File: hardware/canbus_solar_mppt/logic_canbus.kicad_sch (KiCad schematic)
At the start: 29 parts

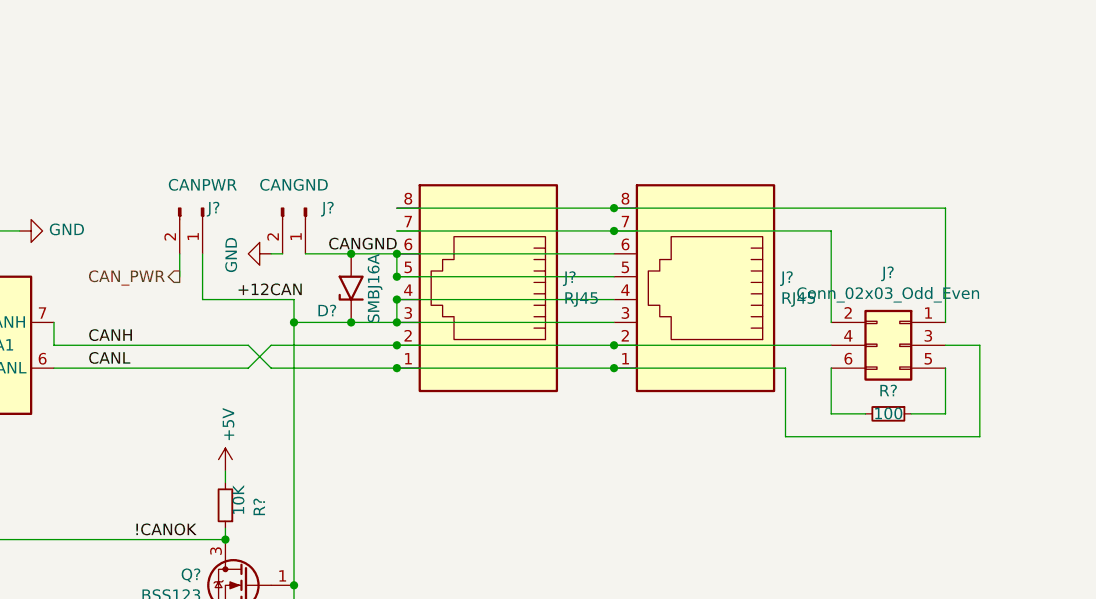
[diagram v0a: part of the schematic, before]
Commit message: Add feedthrough capacitors as EMI filters on power inputs
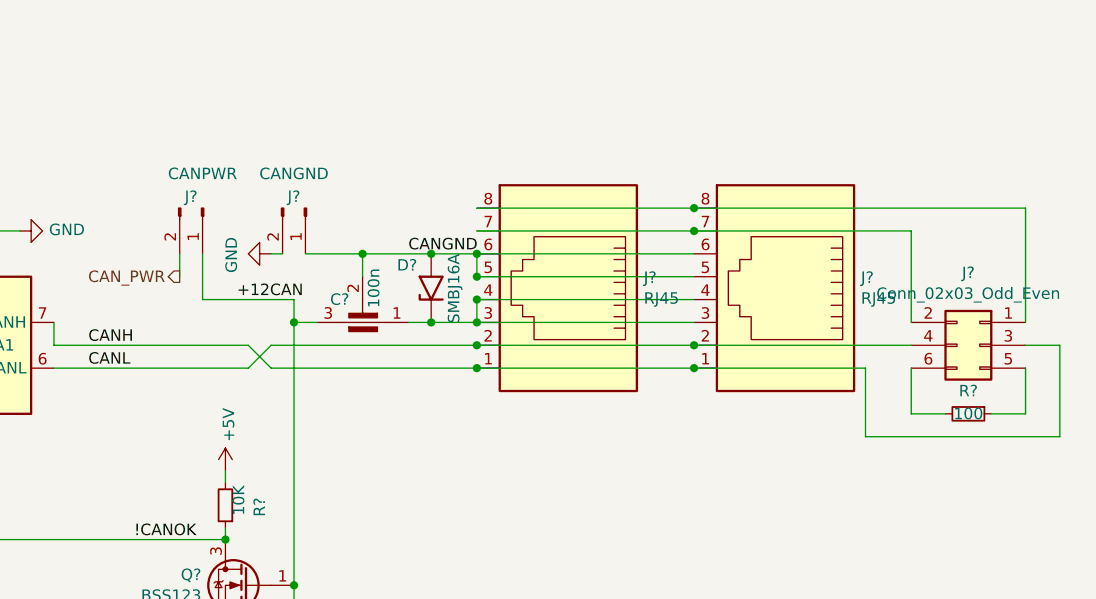
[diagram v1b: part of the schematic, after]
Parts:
- added C?: 100n, local:C_filter_0805, symbol Device:C_Feedthrough
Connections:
- net +12CAN: now also C?.3; no longer D?.1 (A1), J?.3, J?.3, J?.4, J?.4
- net CANGND: now also C?.2
- new net: C?.1, D?.1 (A1), J?.3, J?.3, J?.4, J?.4
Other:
- moved on the sheet: D?, J?, R?

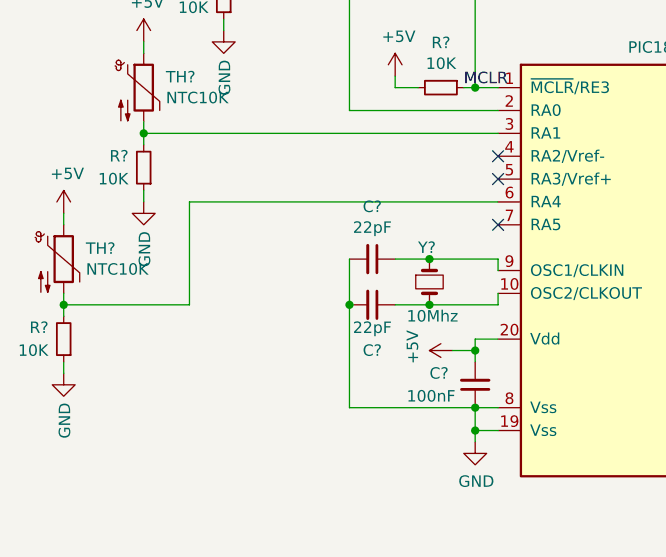
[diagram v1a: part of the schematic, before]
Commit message: Add a voltage reference for the pic18 comparator, and a matching voltage divider at DC/DC output.
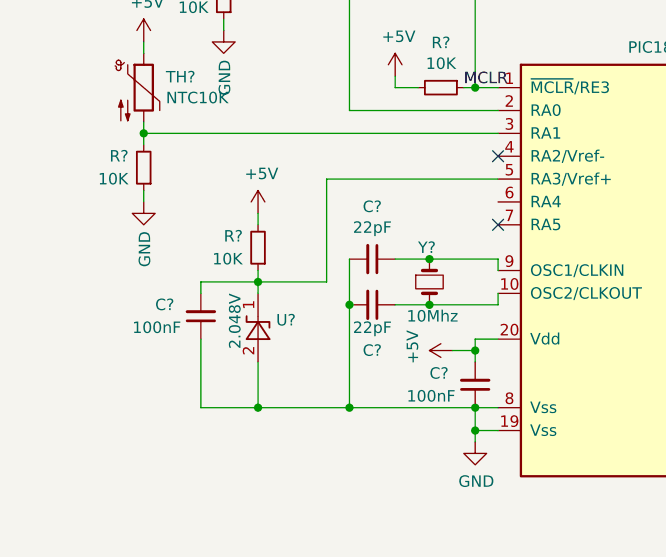
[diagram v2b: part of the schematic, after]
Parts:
- removed R?: 10K, Resistor_SMD:R_1206_3216Metric_Pad1.30x1.75mm_HandSolder, symbol Device:R_Small
- removed TH?: NTC10K, TerminalBlock_TE-Connectivity:TerminalBlock_TE_282834-2_1x02_P2.54mm_Horizontal, symbol Device:Thermistor_NTC
- added C?: 100nF, Capacitor_SMD:C_0805_2012Metric_Pad1.18x1.45mm_HandSolder, symbol Device:C_Small
- added R?: 10K, Resistor_SMD:R_1206_3216Metric_Pad1.30x1.75mm_HandSolder, symbol Device:R_Small
- added U?: 2.048V, Package_TO_SOT_SMD:SOT-23, symbol Reference_Voltage:LM4040DBZ-2.0
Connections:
- net +5V: now also R?.2
- net GND: now also C?.1, U?.2 (A)
- net at U?.5 (RA3/Vref+): now also C?.2, R?.1, U?.1 (K)
- no-connect marks 3 -> 2

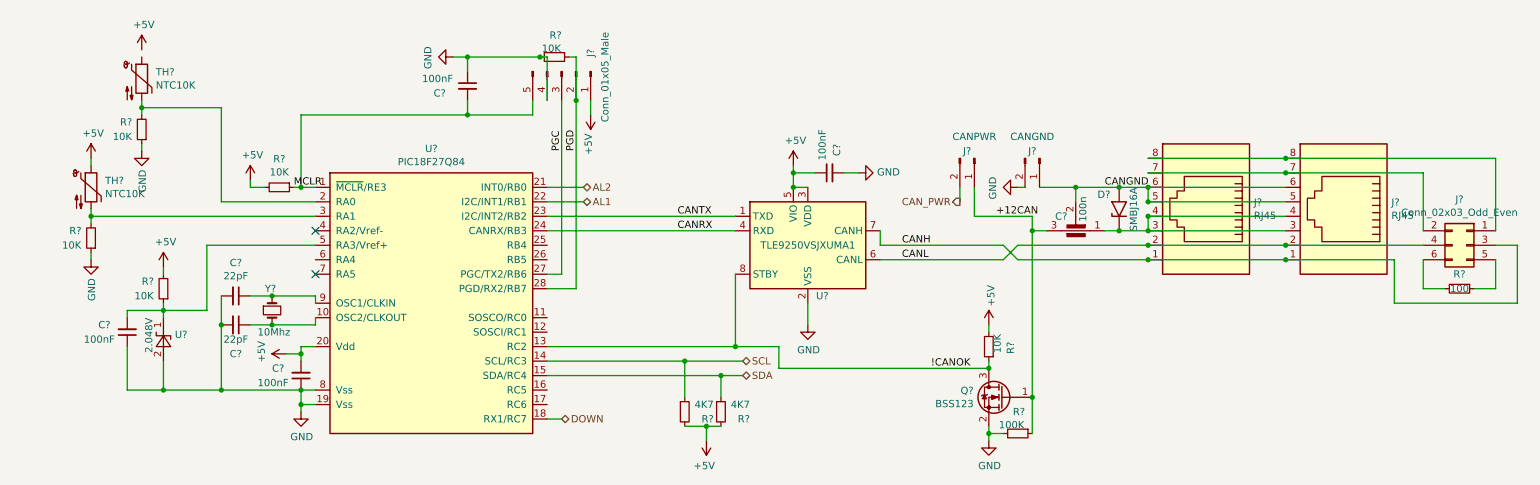
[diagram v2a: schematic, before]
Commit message: Add more signals between pic18 and DC/DC
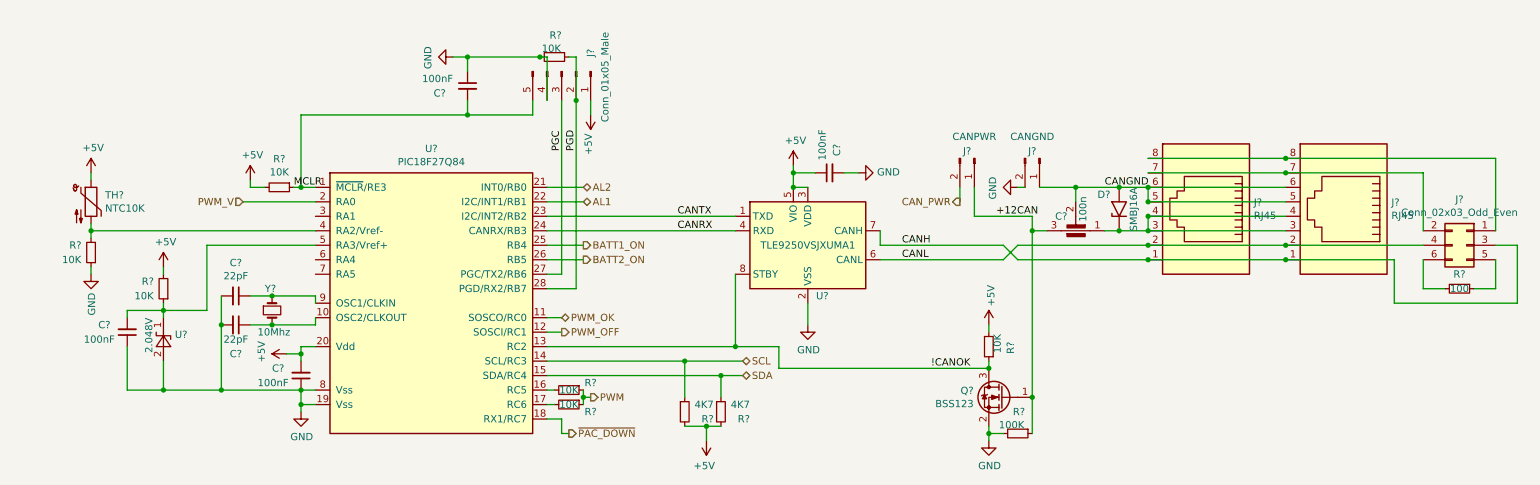
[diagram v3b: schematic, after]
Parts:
- removed R?: 10K, Resistor_SMD:R_1206_3216Metric_Pad1.30x1.75mm_HandSolder, symbol Device:R_Small
- removed TH?: NTC10K, TerminalBlock_TE-Connectivity:TerminalBlock_TE_282834-2_1x02_P2.54mm_Horizontal, symbol Device:Thermistor_NTC
- added R? (x2): 10K, Resistor_THT:R_Axial_DIN0207_L6.3mm_D2.5mm_P7.62mm_Horizontal, symbol Device:R_Small
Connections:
- net PWM_OK: now reaches U?.11 (SOSCO/RC0)
- net PWM_OFF: now reaches U?.12 (SOSCI/RC1)
- net at U?.16 (RC5): now also R?.2
- net at U?.17 (RC6): now also R?.2
- net PWM_V: now reaches U?.2 (RA0)
- net BATT1_ON: now reaches U?.25 (RB4)
- net BATT2_ON: now reaches U?.26 (RB5)
- net at R?.2, TH?.2: now also U?.4 (RA2/Vref-); no longer U?.3 (RA1)
- net DOWN renamed ~{PAC_DOWN}
- new net PWM: R?.1, R?.1
- no-connect marks 2 -> 0
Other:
- moved on the sheet: R?, TH?

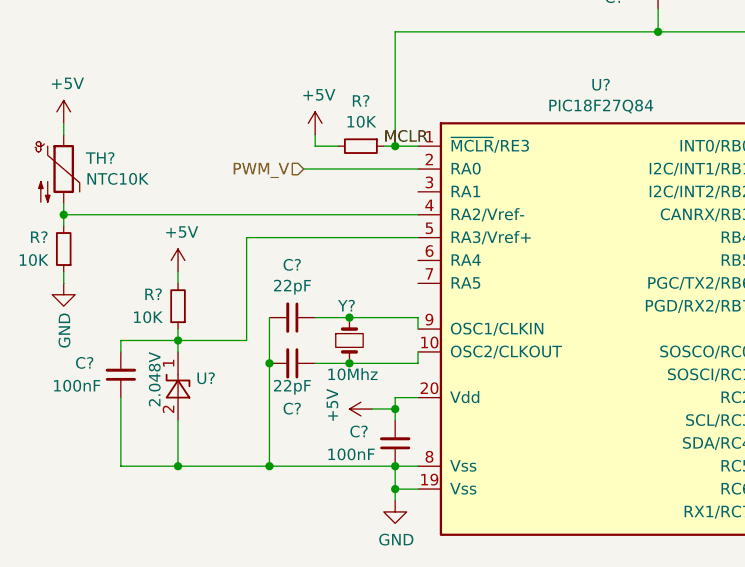
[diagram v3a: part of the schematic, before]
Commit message: Add MCOB12864JX oled display. I2C-connected, not enough pic18 pins for SPI ...
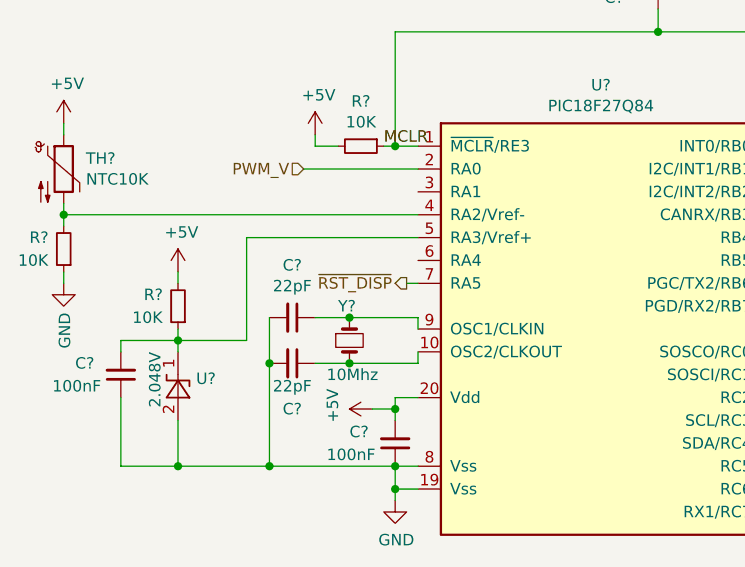
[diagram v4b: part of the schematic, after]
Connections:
- net ~{RST_DISP}: now reaches U?.7 (RA5)
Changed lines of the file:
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@@
+    (stroke (width 0) (type default) (color 0 0 0 0))
+  )
+  (wire (pts (xy 69.85 87.63) (xy 71.12 87.63))
     (stroke (width 0) (type default) (color 0 0 0 0))
   )
@@
     (effects (font (size 1.27 1.27)) (justify left))
   )
+  (hierarchical_label "~{RST_DISP}" (shape output) (at 69.85 87.63 180)
+    (effects (font (size 1.27 1.27)) (justify right))
+  )
   (hierarchical_label "SDA" (shape bidirectional) (at 146.05 105.41 0)

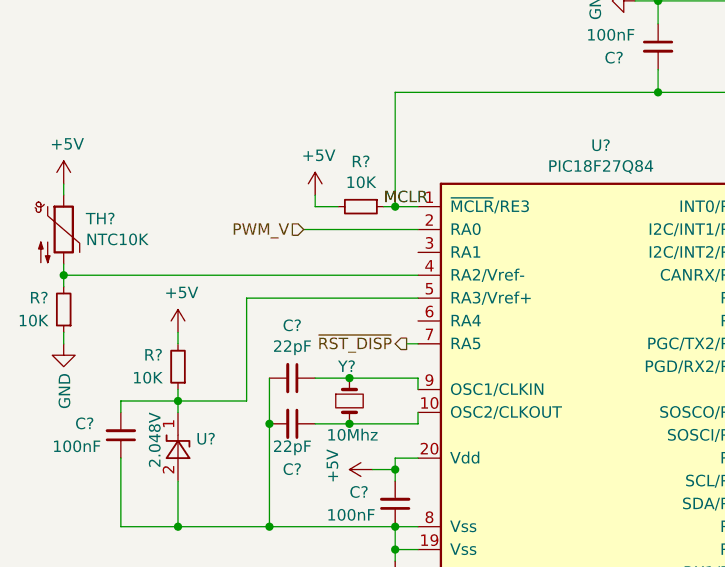
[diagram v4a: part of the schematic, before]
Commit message: Add 2 control buttons (could be more).
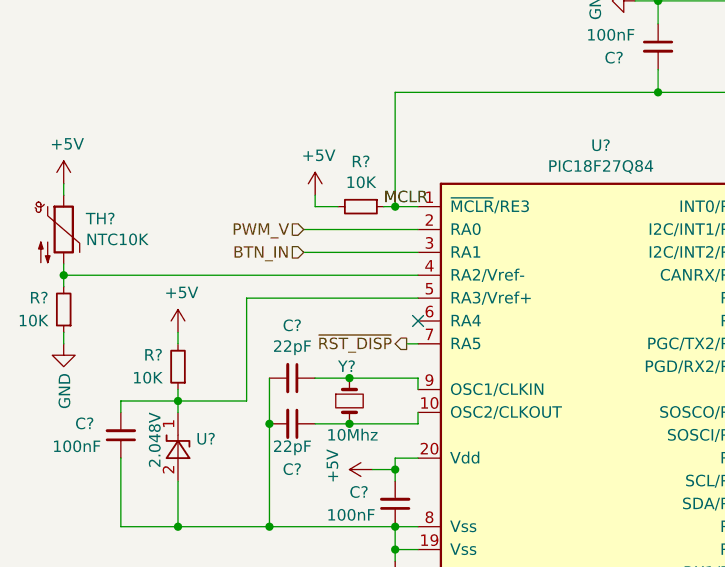
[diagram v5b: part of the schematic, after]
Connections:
- net BTN_IN: now reaches U?.3 (RA1)
- no-connect marks 0 -> 1
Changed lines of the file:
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@@
   (junction (at 68.58 107.95) (diameter 0) (color 0 0 0 0)
   )
+  (no_connect (at 71.12 85.09))
   (wire (pts (xy 111.76 110.49) (xy 113.03 110.49))
     (stroke (width 0) (type default) (color 0 0 0 0))
@@
   )
   (wire (pts (xy 52.07 82.55) (xy 71.12 82.55))
+    (stroke (width 0) (type default) (color 0 0 0 0))
+  )
+  (wire (pts (xy 58.42 77.47) (xy 71.12 77.47))
     (stroke (width 0) (type default) (color 0 0 0 0))
   )
@@
     (effects (font (size 1.27 1.27)) (justify left))
   )
+  (hierarchical_label "BTN_IN" (shape input) (at 58.42 77.47 180)
+    (effects (font (size 1.27 1.27)) (justify right))
+  )
   (hierarchical_label "PWM_V" (shape input) (at 58.42 74.93 180)

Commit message: Use a SMD thermistor
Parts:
- TH?: footprint TerminalBlock_TE-Connectivity:TerminalBlock_TE_282834-2_1x02_P2.54mm_Horizontal -> Resistor_SMD:R_0201_0603Metric_Pad0.64x0.40mm_HandSolder; P/N ND06P00103K/282834-2 -> NT06104F3950B1H
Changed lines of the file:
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@@
       (effects (font (size 1.27 1.27)) (justify left))
     )
-    (property "Footprint" "TerminalBlock_TE-Connectivity:TerminalBlock_TE_282834-2_1x02_P2.54mm_Horizontal" (id 2) (at 31.75 73.66 0)
+    (property "Footprint" "Resistor_SMD:R_0201_0603Metric_Pad0.64x0.40mm_HandSolder" (id 2) (at 31.75 73.66 0)
       (effects (font (size 1.27 1.27)) hide)
     )
@@
       (effects (font (size 1.27 1.27)) hide)
     )
-    (property "P/N" "ND06P00103K/282834-2" (id 4) (at 31.75 74.93 0)
+    (property "P/N" " NT06104F3950B1H " (id 4) (at 31.75 74.93 0)
       (effects (font (size 1.27 1.27)) hide)
     )

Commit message: Add footprint for OLED display annotate schematic run and fix ERC
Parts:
- C31: renamed from C?; value 100n -> 100nF
- gave numbers to parts that had none: 30
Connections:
- net GND: now also U6.6 (RA4)
- no-connect marks 1 -> 0

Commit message: Fix up resistor footprints, use only SMD for now.
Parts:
- R25, R26, R28: footprint Resistor_SMD:R_1206_3216Metric_Pad1.30x1.75mm_HandSolder -> Resistor_SMD:R_0805_2012Metric_Pad1.20x1.40mm_HandSolder
- R27, R29, R30, R31, R32, R33, R34: footprint Resistor_THT:R_Axial_DIN0207_L6.3mm_D2.5mm_P7.62mm_Horizontal -> Resistor_SMD:R_0805_2012Metric_Pad1.20x1.40mm_HandSolder
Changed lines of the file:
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@@
       (effects (font (size 1.27 1.27)) (justify right))
     )
-    (property "Footprint" "Resistor_SMD:R_1206_3216Metric_Pad1.30x1.75mm_HandSolder" (id 2) (at 113.03 49.53 0)
+    (property "Footprint" "Resistor_SMD:R_0805_2012Metric_Pad1.20x1.40mm_HandSolder" (id 2) (at 113.03 49.53 0)
       (effects (font (size 1.27 1.27)) hide)
     )
@@
       (effects (font (size 1.27 1.27)) (justify right))
     )
-    (property "Footprint" "Resistor_THT:R_Axial_DIN0207_L6.3mm_D2.5mm_P7.62mm_Horizontal" (id 2) (at 194.31 115.57 0)
+    (property "Footprint" "Resistor_SMD:R_0805_2012Metric_Pad1.20x1.40mm_HandSolder" (id 2) (at 194.31 115.57 0)
       (effects (font (size 1.27 1.27)) hide)
     )
@@
     (property "Reference" "R27" (id 0) (at 64.77 67.4116 90))
     (property "Value" "10K" (id 1) (at 64.77 69.723 90))
-    (property "Footprint" "Resistor_THT:R_Axial_DIN0207_L6.3mm_D2.5mm_P7.62mm_Horizontal" (id 2) (at 64.77 72.39 0)
+    (property "Footprint" "Resistor_SMD:R_0805_2012Metric_Pad1.20x1.40mm_HandSolder" (id 2) (at 64.77 72.39 0)
       (effects (font (size 1.27 1.27)) hide)
     )
@@
     (property "Reference" "R30" (id 0) (at 119.38 111.76 90))
     (property "Value" "10K" (id 1) (at 115.57 110.49 90))
-    (property "Footprint" "Resistor_THT:R_Axial_DIN0207_L6.3mm_D2.5mm_P7.62mm_Horizontal" (id 2) (at 115.57 110.49 0)
+    (property "Footprint" "Resistor_SMD:R_0805_2012Metric_Pad1.20x1.40mm_HandSolder" (id 2) (at 115.57 110.49 0)
       (effects (font (size 1.27 1.27)) hide)
     )
@@
       (effects (font (size 1.27 1.27)) (justify right))
     )
-    (property "Footprint" "Resistor_SMD:R_1206_3216Metric_Pad1.30x1.75mm_HandSolder" (id 2) (at 44.45 90.17 0)
+    (property "Footprint" "Resistor_SMD:R_0805_2012Metric_Pad1.20x1.40mm_HandSolder" (id 2) (at 44.45 90.17 0)
       (effects (font (size 1.27 1.27)) hide)
     )
@@
       (effects (font (size 1.27 1.27)) (justify right))
     )
-    (property "Footprint" "Resistor_THT:R_Axial_DIN0207_L6.3mm_D2.5mm_P7.62mm_Horizontal" (id 2) (at 135.89 111.76 0)
+    (property "Footprint" "Resistor_SMD:R_0805_2012Metric_Pad1.20x1.40mm_HandSolder" (id 2) (at 135.89 111.76 0)
       (effects (font (size 1.27 1.27)) hide)
     )
@@
       (effects (font (size 1.27 1.27)) (justify right))
     )
-    (property "Footprint" "Resistor_SMD:R_1206_3216Metric_Pad1.30x1.75mm_HandSolder" (id 2) (at 31.75 83.82 0)
+    (property "Footprint" "Resistor_SMD:R_0805_2012Metric_Pad1.20x1.40mm_HandSolder" (id 2) (at 31.75 83.82 0)
       (effects (font (size 1.27 1.27)) hide)
     )
@@
     (property "Reference" "R29" (id 0) (at 119.38 106.68 90))
     (property "Value" "10K" (id 1) (at 115.57 107.95 90))
-    (property "Footprint" "Resistor_THT:R_Axial_DIN0207_L6.3mm_D2.5mm_P7.62mm_Horizontal" (id 2) (at 115.57 107.95 0)
+    (property "Footprint" "Resistor_SMD:R_0805_2012Metric_Pad1.20x1.40mm_HandSolder" (id 2) (at 115.57 107.95 0)
       (effects (font (size 1.27 1.27)) hide)
     )
@@
       (effects (font (size 1.27 1.27)) (justify right))
     )
-    (property "Footprint" "Resistor_THT:R_Axial_DIN0207_L6.3mm_D2.5mm_P7.62mm_Horizontal" (id 2) (at 189.23 100.33 0)
+    (property "Footprint" "Resistor_SMD:R_0805_2012Metric_Pad1.20x1.40mm_HandSolder" (id 2) (at 189.23 100.33 0)
       (effects (font (size 1.27 1.27)) hide)
     )
@@
       (effects (font (size 1.27 1.27)) (justify right))
     )
-    (property "Footprint" "Resistor_THT:R_Axial_DIN0207_L6.3mm_D2.5mm_P7.62mm_Horizontal" (id 2) (at 142.24 111.76 0)
-      (effects (font (size 1.27 1.27)) hide)
-    )
+    (property "Footprint" "Resistor_SMD:R_0805_2012Metric_Pad1.20x1.40mm_HandSolder" (id 2) (at 142.24 111.76 0)
+      (effects (font (size 1.27 1.27)) hide)
+    )
